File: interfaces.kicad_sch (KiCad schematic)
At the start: 30 parts, among them J3 Conn_01x02, J4 Conn_01x02, J5 Conn_01x02, J7 Conn_01x02, SW10 SPST_BTN_A, SW11 SPST_BTN_X, SW12 SPST_BTN_Y, SW3 SPST_DPAD_LEFT, SW4 SPST_BTN_SELECT, SW5 SPST_DPAD_DOWN, SW6 SPST_DPAD_RIGHT, SW7 SPST_DPAD_UP, SW8 SPST_DPAD_START, SW9 SPST_BTN_B, U1 DA7282-00FVC, U4 MCP23017_ML, U7 MAX98357A

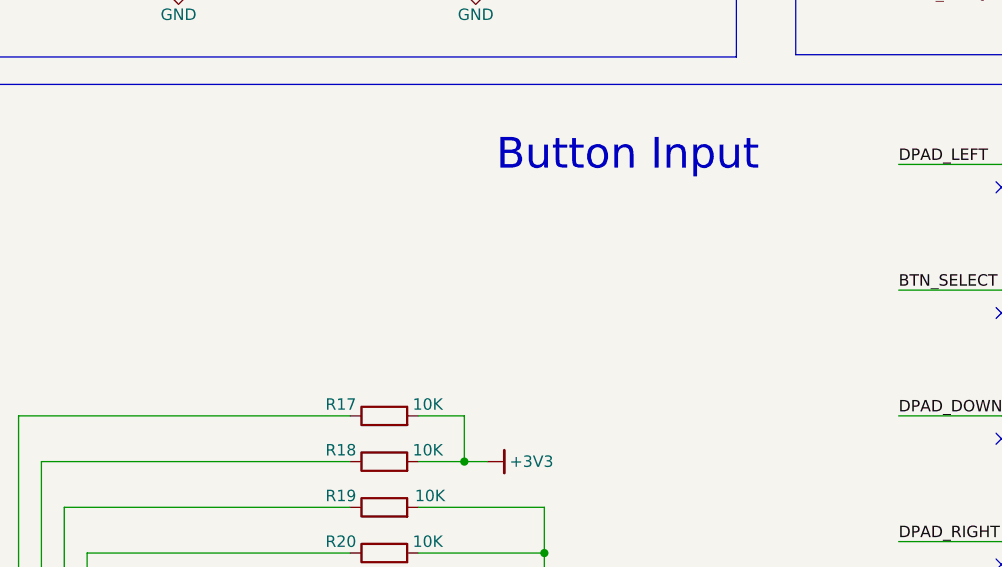
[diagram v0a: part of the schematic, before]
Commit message: Release candidate
Changed USBC connector, changed TagConnect to use footprint with legs, move NRF52 to edge of board, clean up traces
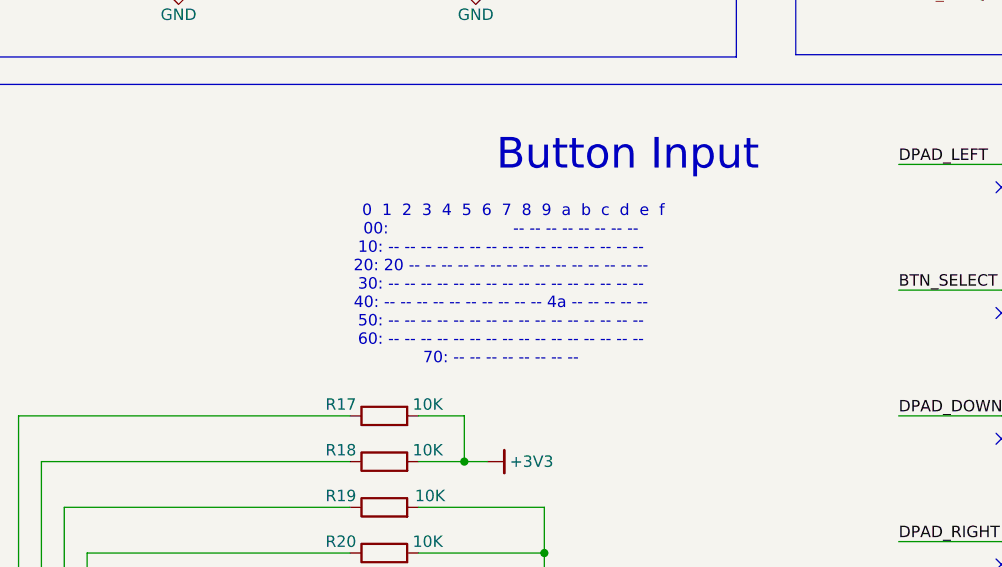
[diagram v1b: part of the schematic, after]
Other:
- note added: "0 1 2 3 4 5 6 7 8 9 a b c d e f 00: -- -- -- -- -- -- -- -- 10: -- -- -- -- -- -- -- -- -- -- -- -- -- -- -- -- 20: 20 -- -- -- -- -- -- -- -- -- -- -- -- -- -- -- 30: -- -- -- -- -- -- -- -- -- -- -- -- -- -- -- -- 40: -- -- -- -- -- -- -- -- -- -- 4a -- -- -- -- -- 50: -- -- -- -- -- -- -- -- -- -- -- -- -- -- -- -- 60: -- -- -- -- -- -- -- -- -- -- -- -- -- -- -- -- 70: -- -- -- -- -- -- -- --"
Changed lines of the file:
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@@
+		)
+	)
+	(text "     0  1  2  3  4  5  6  7  8  9  a  b  c  d  e  f\n00:                         -- -- -- -- -- -- -- --\n10: -- -- -- -- -- -- -- -- -- -- -- -- -- -- -- --\n20: 20 -- -- -- -- -- -- -- -- -- -- -- -- -- -- --\n30: -- -- -- -- -- -- -- -- -- -- -- -- -- -- -- --\n40: -- -- -- -- -- -- -- -- -- -- 4a -- -- -- -- --\n50: -- -- -- -- -- -- -- -- -- -- -- -- -- -- -- --\n60: -- -- -- -- -- -- -- -- -- -- -- -- -- -- -- --\n70: -- -- -- -- -- -- -- --"
+		(exclude_from_sim no)
+		(at 73.914 76.962 0)
+		(effects
+			(font
+				(size 1.27 1.27)
+			)
 		)
 	)

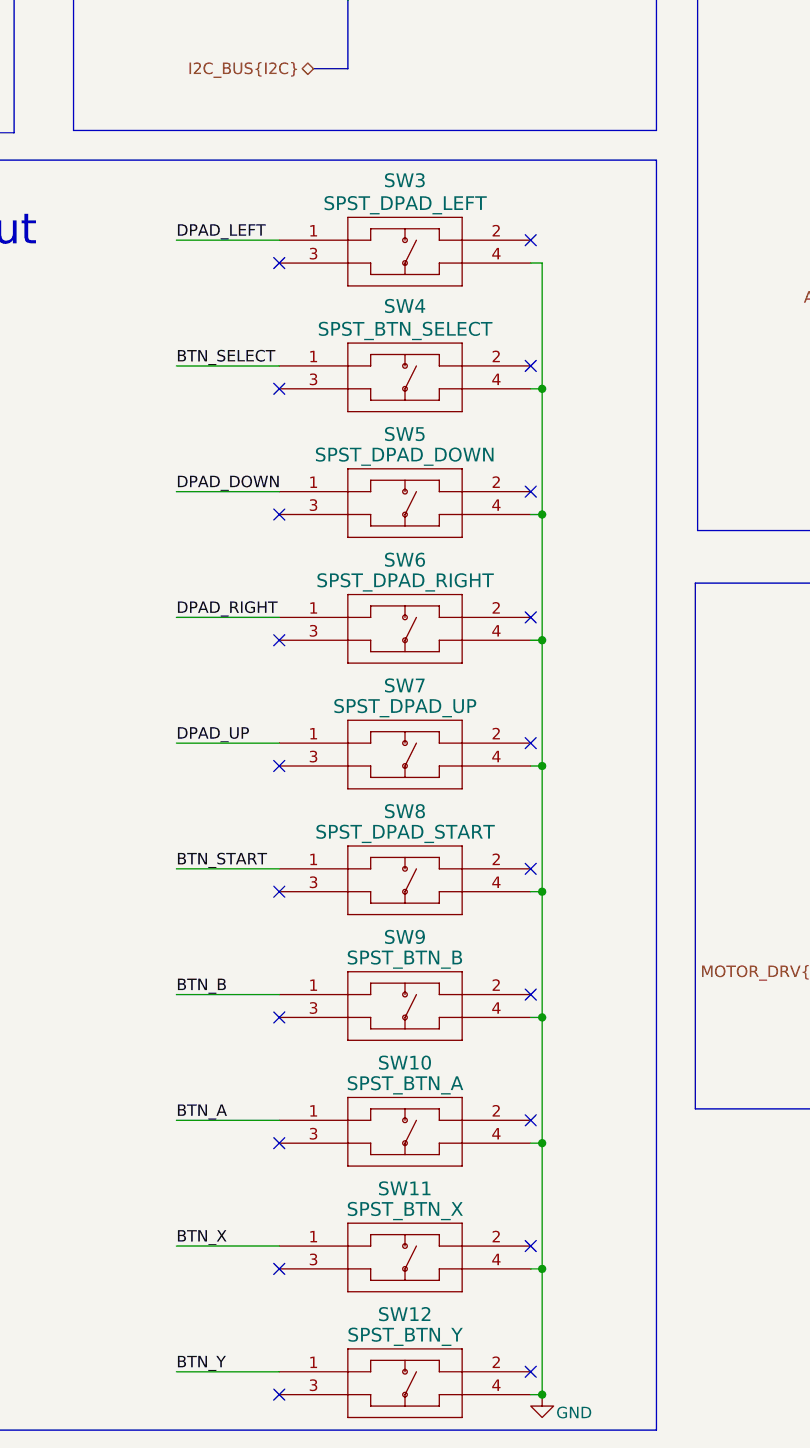
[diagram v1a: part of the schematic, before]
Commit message: Change button footprint
Change button footprint to PTS647 and add a few more stitching vias.
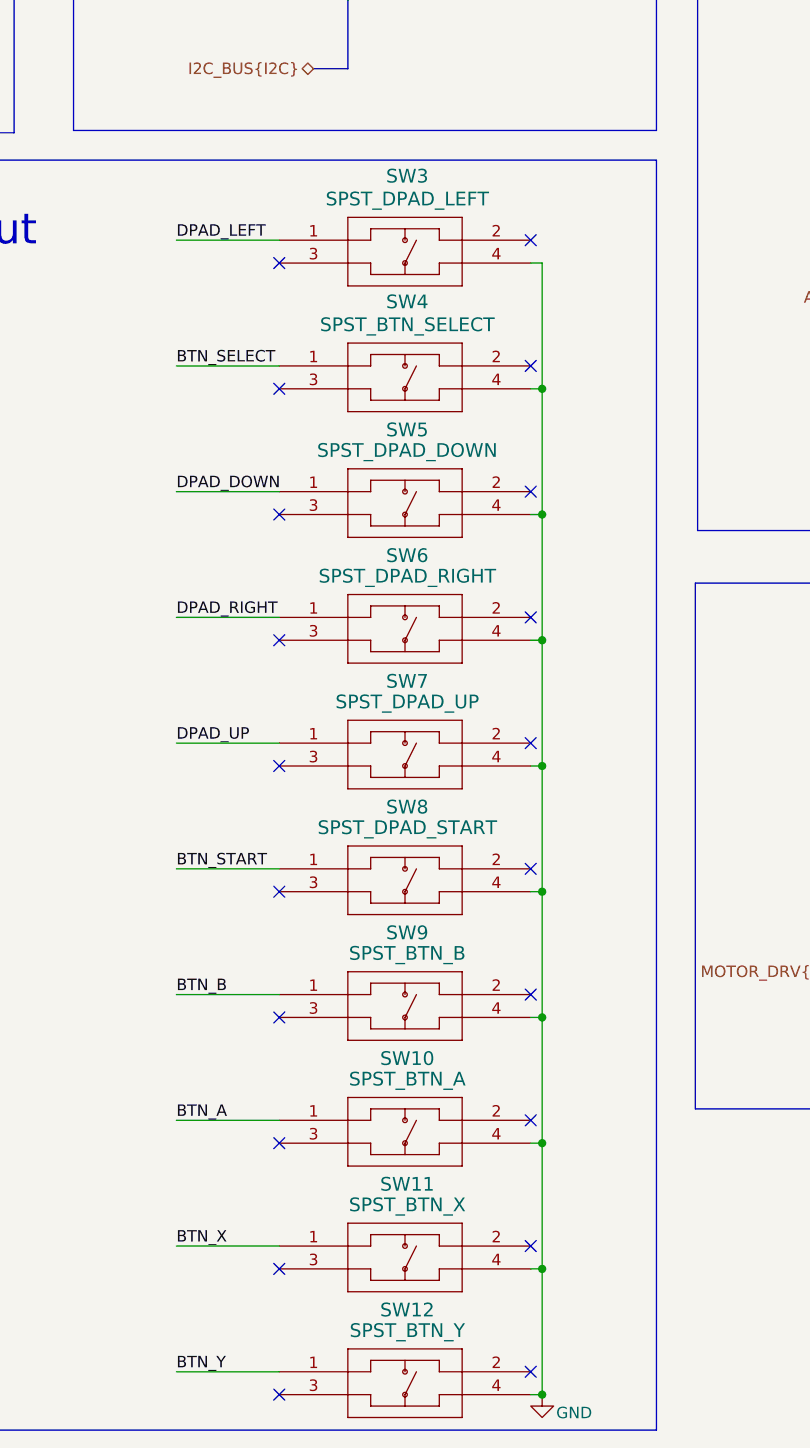
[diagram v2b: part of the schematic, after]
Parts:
- SW10, SW11, SW12, SW3, SW4, SW5, SW6, SW7, SW8, SW9: footprint PTS526_SK15_SMTR2_LFS:SMT_FS -> PTS_647_SN50_SMTR2_LFS:SW_PTS_647_SN50_SMTR2_LFS; symbol PTS526_SK15_SMTR2_LFS:PTS526_SK15_SMTR2_LFS -> PTS_647_SN50_SMTR2_LFS:PTS_647_SN50_SMTR2_LFS; Check_prices (none) -> https://www.snapeda.com/parts/PTS%20647%20SN50%20SMTR2%20LF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; Description_1 (none) -> Tactile Switch SPST-NO Top Actuated Surface Mount; DigiKey_Part_Number (none) -> PTS647SN50SMTR2LFSTR-ND; MANUFACTURER (none) -> C&K; MAXIMUM_PACKAGE_HEIGHT (none) -> 5.0 mm; MF (none) -> C&K; MP PTS526SK15SMTR2 LFS -> PTS647SN50SMTR2 LFS; PARTREV (none) -> 4 Apr 22; Package (none) -> None; SNAPEDA_PN (none) -> PTS 647 SN50 SMTR2 LFS; STANDARD (none) -> Manufacturer Recommendations; SnapEDA_Link (none) -> https://www.snapeda.com/parts/PTS%20647%20SN50%20SMTR2%20LF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

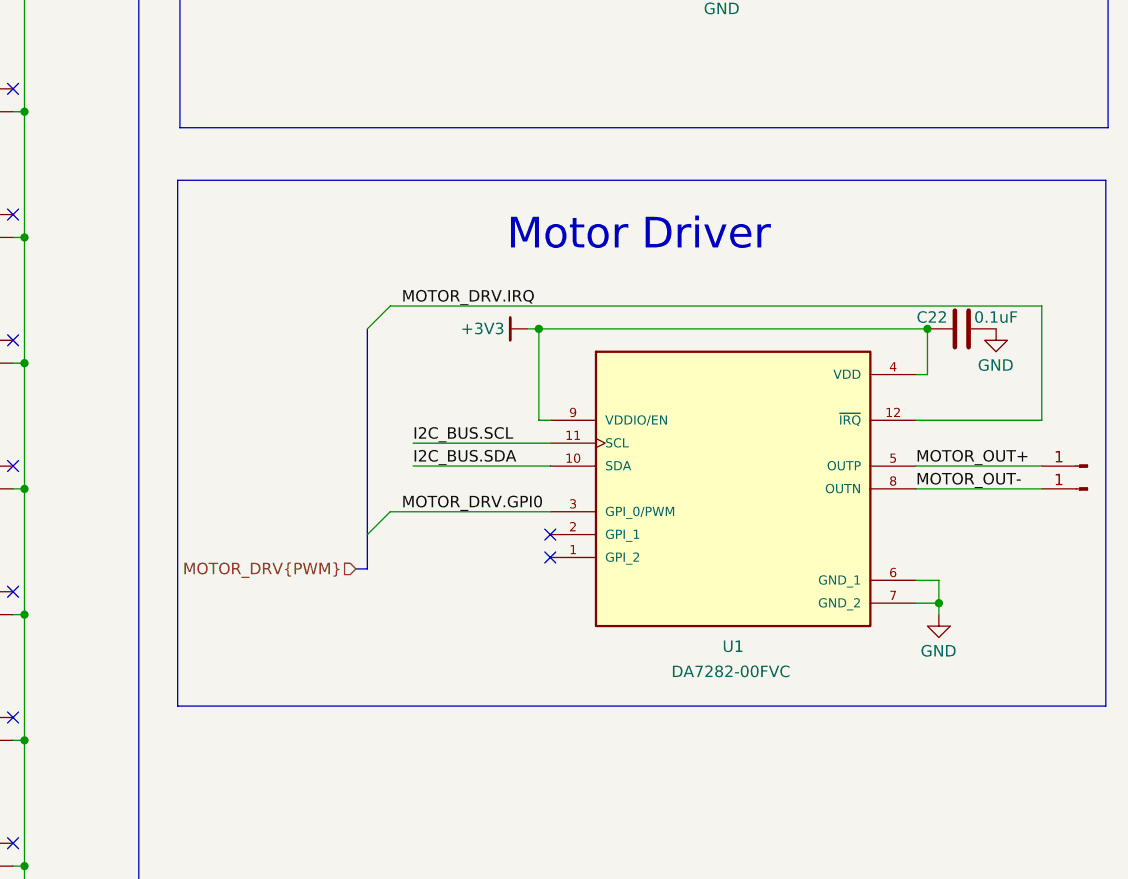
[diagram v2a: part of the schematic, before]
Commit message: Replaced DA7280 with DRV2605
Replaced DA7280 with DRV2605 to simplify board support code in Hack-A-Friend Arduino Library.
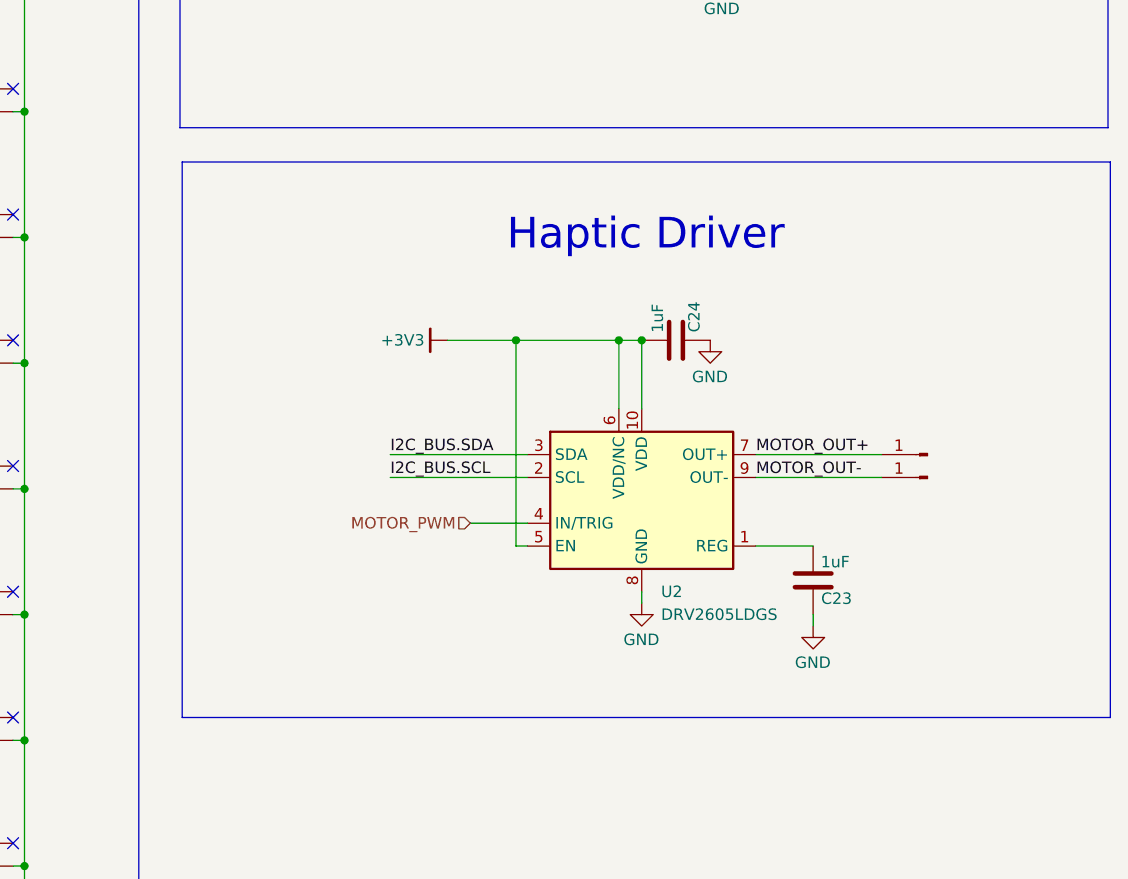
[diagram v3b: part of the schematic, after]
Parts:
- removed C22: 0.1uF, Capacitor_SMD:C_0402_1005Metric, symbol Device:C
- removed U1: DA7282-00FVC, DA7282_00FVC:QFN65P300X300X84-12N, symbol DA7282-00FVC:DA7282-00FVC
- added C23, C24: 1uF, Capacitor_SMD:C_0603_1608Metric, symbol Device:C
- added U2: DRV2605LDGS, Package_SO:VSSOP-10_3x3mm_P0.5mm, symbol Driver_Haptic:DRV2605LDGS
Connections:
- net +3V3: now also C24.2, U2.10 (VDD), U2.5 (EN), U2.6 (VDD/NC)
- net GND: now also C23.1, C24.1, U2.8 (GND)
- net I2C_BUS.SCL: now also U2.2 (SCL)
- net I2C_BUS.SDA: now also U2.3 (SDA)
- net MOTOR_OUT+: now also U2.7 (OUT+)
- net MOTOR_OUT-: now also U2.9 (OUT-)
- new net: C23.2, U2.1 (REG)
- new net MOTOR_PWM: U2.4 (IN/TRIG)
- no-connect marks 22 -> 20
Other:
- note added: "Haptic Driver"
- note removed: "Motor Driver"

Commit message: Added MP part number fields to schematic and PCB design,
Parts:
- U2: MP (none) -> DRV2605LDGSR
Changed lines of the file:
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@@
+			)
+		)
+		(property "MP" "DRV2605LDGSR"
+			(at 227.33 137.16 0)
+			(effects
+				(font
+					(size 1.27 1.27)
+				)
+				(hide yes)
 			)
 		)
